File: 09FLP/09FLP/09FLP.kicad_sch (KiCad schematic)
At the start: 51 parts, among them J1 Floppy, J2 Floppy, J3 Floppy_50p, Q1 BS170, Q2 BS170, U1 74HC245, U13 74LS273, U2 GAL16V8, U3 WD2793, U4 74LS240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

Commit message: FLP schematic ch.
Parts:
- C3: value 22u -> 220n

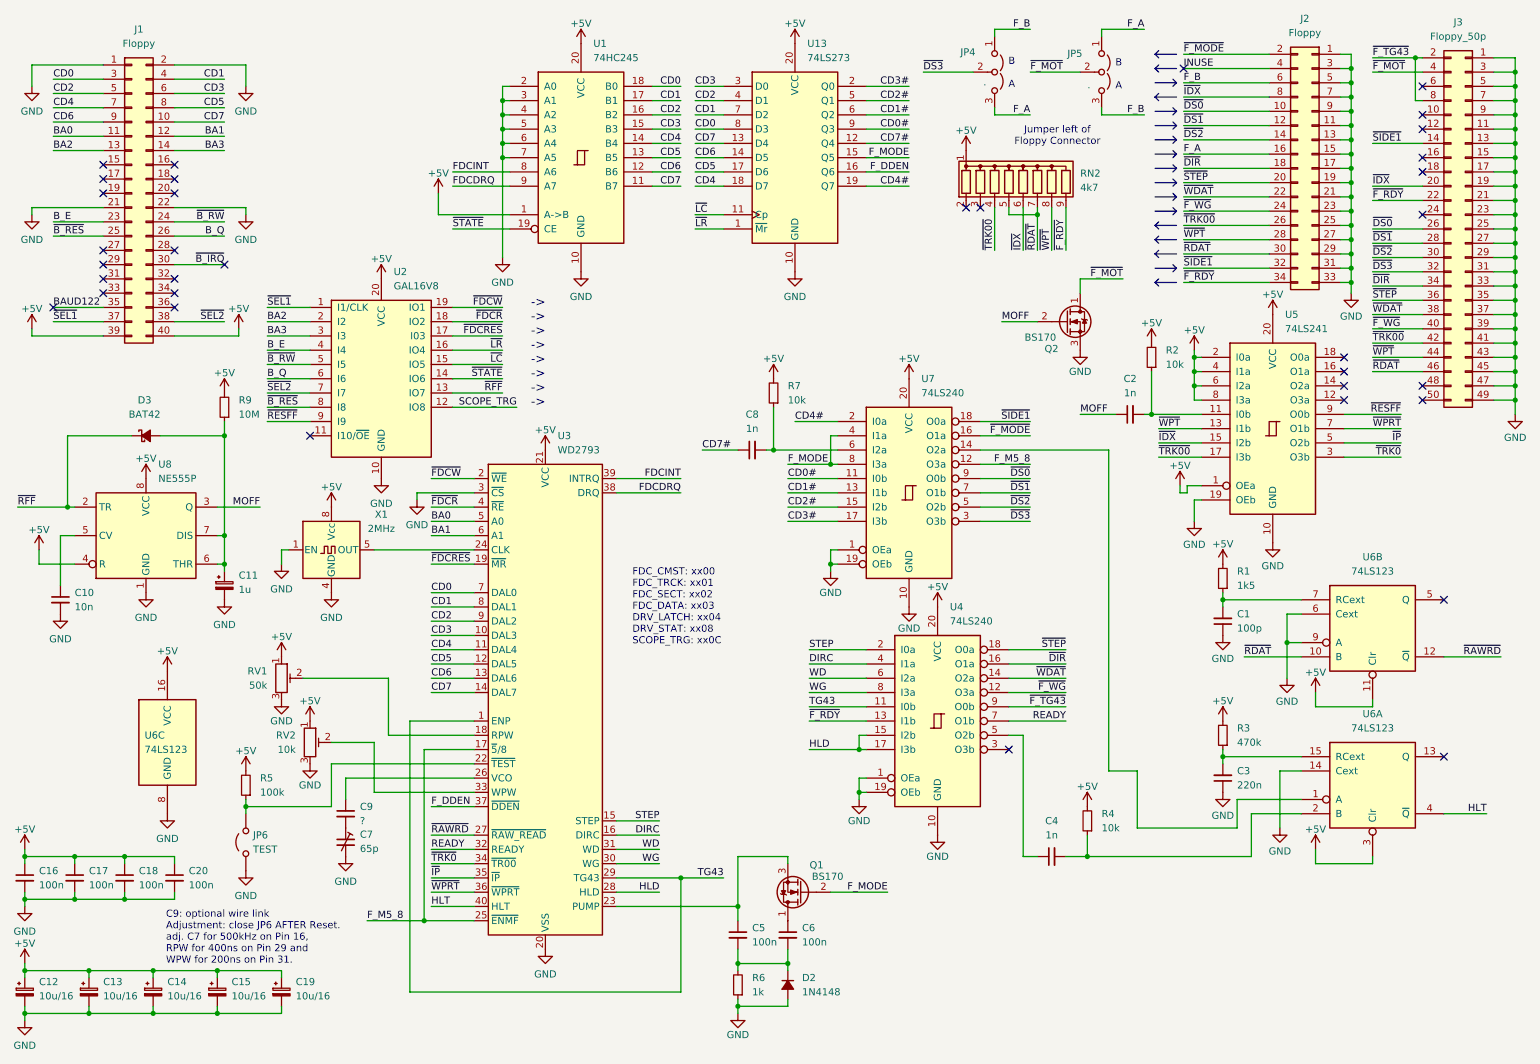
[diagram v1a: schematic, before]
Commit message: 09NET added, 09FLP minor ch.
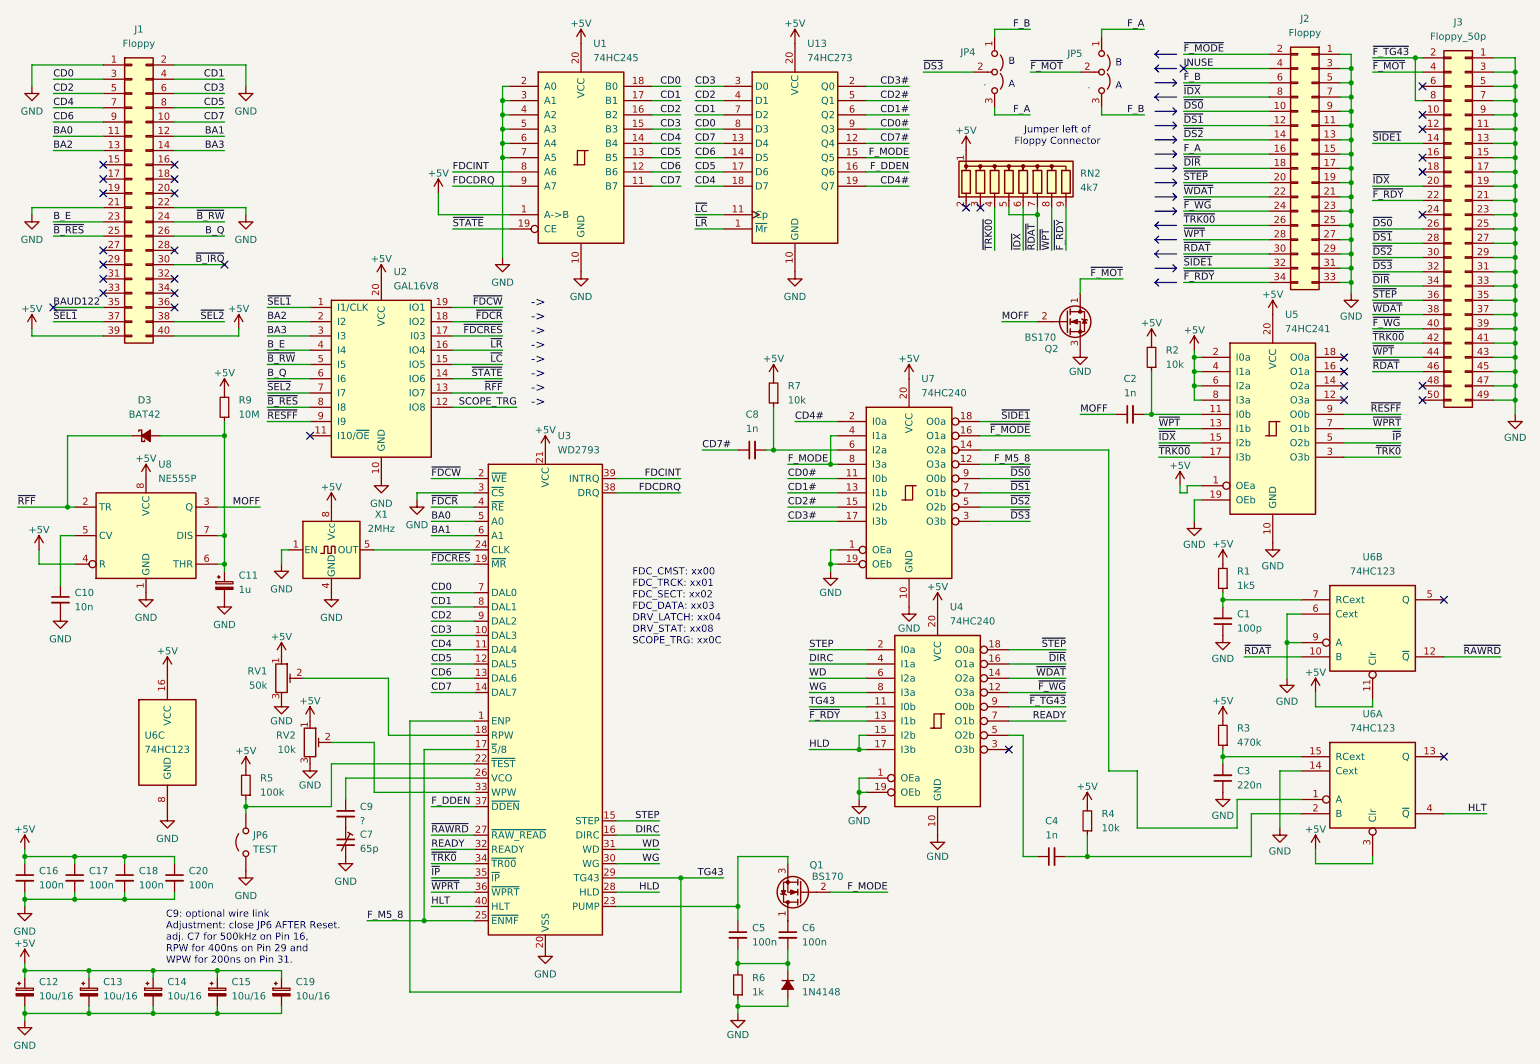
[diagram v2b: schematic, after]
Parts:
- U13: value 74LS273 -> 74HC273
- U4, U7: value 74LS240 -> 74HC240
- U5: value 74LS241 -> 74HC241
- U6: value 74LS123 -> 74HC123
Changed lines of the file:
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@@
 		(company "100% Offner")
 		(comment 1 "redraw from kees1948 FLEX and UniFLEX System")
-		(comment 2 "v1.1: ch. C3")
+		(comment 2 "v1.1: ch. C3, ch. all 74LS Types to HC")
 	)
 	(junction
@@
 			)
 		)
-		(property "Value" "74LS241"
+		(property "Value" "74HC241"
 			(at 240.9541 68.58 0)
 			(effects
@@
 			)
 		)
-		(property "Value" "74LS240"
+		(property "Value" "74HC240"
 			(at 181.2641 120.65 0)
 			(effects
@@
 			)
 		)
-		(property "Value" "74LS123"
+		(property "Value" "74HC123"
 			(at 256.54 111.76 0)
 			(effects
@@
 			)
 		)
-		(property "Value" "74LS240"
+		(property "Value" "74HC240"
 			(at 176.1841 80.01 0)
 			(effects
@@
 			)
 		)
-		(property "Value" "74LS123"
+		(property "Value" "74HC123"
 			(at 37.846 143.51 0)
 			(effects
@@
 			)
 		)
-		(property "Value" "74LS273"
+		(property "Value" "74HC273"
 			(at 155.8641 20.32 0)
 			(effects
@@
 			)
 		)
-		(property "Value" "74LS123"
+		(property "Value" "74HC123"
 			(at 256.54 139.7 0)
 			(effects

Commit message: Documentation upgrade
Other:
- note added: "C9: optional wire link Adjustment: close JP6 AFTER Reset. adj. C7 for 500kHz on Pin 16, RPW for 250ns on Pin 29 and WPW for 125ns on Pin 31."
- note removed: "C9: optional wire link Adjustment: close JP6 AFTER Reset. adj. C7 for 500kHz on Pin 16, RPW for 400ns on Pin 29 and WPW for 200ns on Pin 31."
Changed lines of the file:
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@@
 		(title "09FLP")
 		(date "2025-02-01")
-		(rev "v1.1")
+		(rev "v1.11")
 		(company "100% Offner")
 		(comment 1 "redraw from kees1948 FLEX and UniFLEX System")
 		(comment 2 "v1.1: ch. C3, ch. all 74LS Types to HC")
+		(comment 3 "v1.11: Direction of J2 Pin 2 ch., Instructions updated")
 	)
 	(junction
@@
 		)
 	)
+	(polyline
+		(pts
+			(xy 220.98 25.4) (xy 220.98 25.4)
+		)
+		(stroke
+			(width 0)
+			(type default)
+		)
+	)
 	(wire
 		(pts
@@
 		)
 	)
+	(polyline
+		(pts
+			(xy 221.7638 19.6471) (xy 221.1288 19.0121)
+		)
+		(stroke
+			(width 0)
+			(type default)
+		)
+	)
 	(wire
 		(pts
@@
 		)
 	)
+	(polyline
+		(pts
+			(xy 221.1288 20.2821) (xy 221.1288 20.2821)
+		)
+		(stroke
+			(width 0)
+			(type default)
+		)
+	)
 	(wire
 		(pts
@@
 		)
 	)
+	(polyline
+		(pts
+			(xy 221.7638 19.6471) (xy 217.9538 19.6471)
+		)
+		(stroke
+			(width 0)
+			(type default)
+		)
+	)
 	(wire
 		(pts
@@
 		)
 	)
-	(polyline
-		(pts
-			(xy 217.805 19.685) (xy 221.615 19.685)
-		)
-		(stroke
-			(width 0)
-			(type default)
-		)
-	)
 	(wire
 		(pts
@@
 		)
 	)
+	(polyline
+		(pts
+			(xy 221.7638 19.6471) (xy 221.1288 20.2821)
+		)
+		(stroke
+			(width 0)
+			(type default)
+		)
+	)
 	(wire
 		(pts
@@
 		)
 	)
+	(polyline
+		(pts
+			(xy 220.98 25.4) (xy 220.98 25.4)
+		)
+		(stroke
+			(width 0)
+			(type default)
+		)
+	)
 	(wire
 		(pts
@@
 		)
 	)
+	(polyline
+		(pts
+			(xy 221.1288 20.2821) (xy 221.1288 20.2821)
+		)
+		(stroke
+			(width 0)
+			(type default)
+		)
+	)
 	(wire
 		(pts
@@
 		)
 	)
-	(polyline
-		(pts
-			(xy 217.805 19.685) (xy 218.44 20.32)
-		)
-		(stroke
-			(width 0)
-			(type default)
-		)
-	)
 	(wire
 		(pts
@@
 		)
 	)
-	(polyline
-		(pts
-			(xy 217.805 19.685) (xy 218.44 19.05)
-		)
-		(stroke
-			(width 0)
-			(type default)
-		)
-	)
 	(wire
 		(pts
@@
 		)
 	)
-	(text "C9: optional wire link\nAdjustment: close JP6 AFTER Reset.\nadj. C7 for 500kHz on Pin 16,\nRPW for 400ns on Pin 29 and\nWPW for 200ns on Pin 31."
+	(text "C9: optional wire link\nAdjustment: close JP6 AFTER Reset.\nadj. C7 for 500kHz on Pin 16,\nRPW for 250ns on Pin 29 and\nWPW for 125ns on Pin 31."
 		(exclude_from_sim no)
 		(at 41.656 177.038 0)
